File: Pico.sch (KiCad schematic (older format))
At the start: 5 parts, among them SW2801 SWITCH TACTILE SPST-NO 50MA 1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, U2801 Pico-JER

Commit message: Added PCA9745B16B. Updated schematic. ERC Passes.
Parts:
- U2801: symbol TMPCB_R2:Pico-JER -> Macro-Keyboard-rescue:Pico-JER-TMPCB_R2
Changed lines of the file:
@@
 L power:GND #PWR02809
 U 1 1 61A68B88
-P 6300 2850
-F 0 "#PWR02809" H 6300 2600 50  0001 C CNN
-F 1 "GND" V 6305 2722 50  0000 R CNN
-F 2 "" H 6300 2850 50  0001 C CNN
-F 3 "" H 6300 2850 50  0001 C CNN
-	1    6300 2850
+P 6650 2850
+F 0 "#PWR02809" H 6650 2600 50  0001 C CNN
+F 1 "GND" V 6655 2722 50  0000 R CNN
+F 2 "" H 6650 2850 50  0001 C CNN
+F 3 "" H 6650 2850 50  0001 C CNN
+	1    6650 2850
 	0    -1   -1   0
 $EndComp
@@
 	7500 3050 7500 2450
 Connection ~ 7500 3050
-Wire Wire Line
-	8200 2450 8200 2650
-Wire Wire Line
-	6300 2650 8200 2650
-Connection ~ 8200 2650
-Wire Wire Line
-	8200 2650 8200 3200
-$Comp
-L TMPCB_R2:Pico-JER U2801
+$Comp
+L Macro-Keyboard-rescue:Pico-JER-TMPCB_R2 U2801
 U 1 1 61A62316
 P 5600 3600
@@
 	0    -1   -1   0
 $EndComp
+Wire Wire Line
+	8200 2450 8200 2650
+Wire Wire Line
+	6300 2650 8200 2650
+Connection ~ 8200 2650
+Wire Wire Line
+	8200 2650 8200 3200
+Wire Wire Line
+	6300 2850 6550 2850
+$Comp
+L power:PWR_FLAG #FLG0101
+U 1 1 61A44DE2
+P 6550 2850
+F 0 "#FLG0101" H 6550 2925 50  0001 C CNN
+F 1 "PWR_FLAG" H 6550 3000 50  0000 C CNN
+F 2 "" H 6550 2850 50  0001 C CNN
+F 3 "~" H 6550 2850 50  0001 C CNN
+	1    6550 2850
+	1    0    0    -1
+$EndComp
+Connection ~ 6550 2850
+Wire Wire Line
+	6550 2850 6650 2850
 $EndSCHEMATC

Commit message: fixed broken schematics becuase of deleted rescue files. ECA passes.
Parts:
- U2801: symbol Macro-Keyboard-rescue:Pico-JER-TMPCB_R2 -> TMPCB_R2:Pico-JER
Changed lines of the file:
@@
 Connection ~ 7500 3050
 $Comp
-L Macro-Keyboard-rescue:Pico-JER-TMPCB_R2 U2801
+L TMPCB_R2:Pico-JER U2801
 U 1 1 61A62316
 P 5600 3600
+AR Path="/61A62316" Ref="U2801"  Part="1"
+AR Path="/61A0B536/61A62316" Ref="U2801"  Part="1"
 F 0 "U2801" H 6100 4750 50  0000 C CNN
 F 1 "Pico-JER" H 5050 4750 50  0000 C CNN
@@
 	8200 2650 8200 3200
 Wire Wire Line
-	6300 2850 6550 2850
+	6300 2850 6500 2850
 $Comp
-L power:PWR_FLAG #FLG0101
-U 1 1 61A44DE2
-P 6550 2850
-F 0 "#FLG0101" H 6550 2925 50  0001 C CNN
-F 1 "PWR_FLAG" H 6550 3000 50  0000 C CNN
-F 2 "" H 6550 2850 50  0001 C CNN
-F 3 "~" H 6550 2850 50  0001 C CNN
-	1    6550 2850
+L power:PWR_FLAG #FLG?
+U 1 1 61A20D92
+P 6500 2850
+F 0 "#FLG?" H 6500 2925 50  0001 C CNN
+F 1 "PWR_FLAG" H 6500 3023 50  0000 C CNN
+F 2 "" H 6500 2850 50  0001 C CNN
+F 3 "~" H 6500 2850 50  0001 C CNN
+	1    6500 2850
 	1    0    0    -1
 $EndComp
-Connection ~ 6550 2850
+Connection ~ 6500 2850
 Wire Wire Line
-	6550 2850 6650 2850
+	6500 2850 6650 2850
 $EndSCHEMATC

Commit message: initial layout
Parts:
- U2801: footprint RPi_Pico:RPi_Pico_SMD_TH -> TMPPCB_R2:RPi_Pico_SMD_TH-JER
- renumbered C2802 to C2801, C2803 to C2802
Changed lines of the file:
@@
 $EndDescr
 $Comp
-L power:GND #PWR02804
+L power:GND #PWR02801
 U 1 1 61A645F3
 P 4900 2850
-F 0 "#PWR02804" H 4900 2600 50  0001 C CNN
+F 0 "#PWR02801" H 4900 2600 50  0001 C CNN
 F 1 "GND" V 4905 2722 50  0000 R CNN
 F 2 "" H 4900 2850 50  0001 C CNN
@@
 $EndComp
 $Comp
-L power:GND #PWR02805
+L power:GND #PWR02802
 U 1 1 61A67A97
 P 4900 3350
-F 0 "#PWR02805" H 4900 3100 50  0001 C CNN
+F 0 "#PWR02802" H 4900 3100 50  0001 C CNN
 F 1 "GND" V 4905 3222 50  0000 R CNN
 F 2 "" H 4900 3350 50  0001 C CNN
@@
 $EndComp
 $Comp
-L power:GND #PWR02806
+L power:GND #PWR02803
 U 1 1 61A67DF9
 P 4900 3850
-F 0 "#PWR02806" H 4900 3600 50  0001 C CNN
+F 0 "#PWR02803" H 4900 3600 50  0001 C CNN
 F 1 "GND" V 4905 3722 50  0000 R CNN
 F 2 "" H 4900 3850 50  0001 C CNN
@@
 $EndComp
 $Comp
-L power:GND #PWR02807
+L power:GND #PWR02804
 U 1 1 61A681A5
 P 4900 4350
-F 0 "#PWR02807" H 4900 4100 50  0001 C CNN
+F 0 "#PWR02804" H 4900 4100 50  0001 C CNN
 F 1 "GND" V 4905 4222 50  0000 R CNN
 F 2 "" H 4900 4350 50  0001 C CNN
@@
 $EndComp
 $Comp
-L power:GND #PWR02808
+L power:GND #PWR02805
 U 1 1 61A6852A
 P 5600 4750
-F 0 "#PWR02808" H 5600 4500 50  0001 C CNN
+F 0 "#PWR02805" H 5600 4500 50  0001 C CNN
 F 1 "GND" H 5605 4577 50  0000 C CNN
 F 2 "" H 5600 4750 50  0001 C CNN
@@
 $EndComp
 $Comp
-L power:GND #PWR02811
+L power:GND #PWR02807
 U 1 1 61A69385
 P 6300 3850
-F 0 "#PWR02811" H 6300 3600 50  0001 C CNN
+F 0 "#PWR02807" H 6300 3600 50  0001 C CNN
 F 1 "GND" V 6305 3722 50  0000 R CNN
 F 2 "" H 6300 3850 50  0001 C CNN
@@
 $EndComp
 $Comp
-L power:GND #PWR02812
+L power:GND #PWR02808
 U 1 1 61A69B7B
 P 6300 4350
-F 0 "#PWR02812" H 6300 4100 50  0001 C CNN
+F 0 "#PWR02808" H 6300 4100 50  0001 C CNN
 F 1 "GND" V 6305 4222 50  0000 R CNN
 F 2 "" H 6300 4350 50  0001 C CNN
@@
 NoConn ~ 6300 2950
 $Comp
-L power:+3V3 #PWR02813
+L power:+3V3 #PWR02810
 U 1 1 61A6C23F
 P 7500 2450
-F 0 "#PWR02813" H 7500 2300 50  0001 C CNN
+F 0 "#PWR02810" H 7500 2300 50  0001 C CNN
 F 1 "+3V3" H 7515 2623 50  0000 C CNN
 F 2 "" H 7500 2450 50  0001 C CNN
@@
 $EndComp
 $Comp
-L power:GND #PWR02814
+L power:GND #PWR02811
 U 1 1 61A6EB26
 P 7500 3400
-F 0 "#PWR02814" H 7500 3150 50  0001 C CNN
+F 0 "#PWR02811" H 7500 3150 50  0001 C CNN
 F 1 "GND" H 7505 3227 50  0000 C CNN
 F 2 "" H 7500 3400 50  0001 C CNN
@@
 $EndComp
 $Comp
-L power:GND #PWR02817
+L power:GND #PWR02814
 U 1 1 61A6E775
 P 8200 3400
-F 0 "#PWR02817" H 8200 3150 50  0001 C CNN
+F 0 "#PWR02814" H 8200 3150 50  0001 C CNN
 F 1 "GND" H 8205 3227 50  0000 C CNN
 F 2 "" H 8200 3400 50  0001 C CNN
@@
 $EndComp
 $Comp
-L power:+5V #PWR02816
+L power:+5V #PWR02813
 U 1 1 61A6CFBC
 P 8200 2450
-F 0 "#PWR02816" H 8200 2300 50  0001 C CNN
+F 0 "#PWR02813" H 8200 2300 50  0001 C CNN
 F 1 "+5V" H 8215 2623 50  0000 C CNN
 F 2 "" H 8200 2450 50  0001 C CNN
@@
 Connection ~ 7500 3050
 $Comp
-L TMPCB_R2:Pico-JER U2801
+L TMPCB_R2:Pico-JER U?
 U 1 1 61A62316
 P 5600 3600
-AR Path="/61A62316" Ref="U2801"  Part="1"
+AR Path="/61A62316" Ref="U?"  Part="1"
 AR Path="/61A0B536/61A62316" Ref="U2801"  Part="1"
 F 0 "U2801" H 6100 4750 50  0000 C CNN
 F 1 "Pico-JER" H 5050 4750 50  0000 C CNN
-F 2 "RPi_Pico:RPi_Pico_SMD_TH" V 5600 3600 50  0001 C CNN
+F 2 "TMPPCB_R2:RPi_Pico_SMD_TH-JER" V 5600 3600 50  0001 C CNN
 F 3 "https://datasheets.raspberrypi.com/pico/pico-datasheet.pdf" H 5600 3600 50  0001 C CNN
 F 4 "2648-SC0915CT-ND" H 5600 3600 50  0001 C CNN "Digikey PN"
@@
 NoConn ~ 6300 2750
 $Comp
-L Device:C_Small C2802
+L Device:C_Small C2801
 U 1 1 61A6E1D1
 P 7500 3300
-F 0 "C2802" H 7592 3346 50  0000 L CNN
+F 0 "C2801" H 7592 3346 50  0000 L CNN
 F 1 "1 uF 10% 10V" H 7592 3255 50  0000 L CNN
 F 2 "Capacitor_SMD:C_0805_2012Metric_Pad1.18x1.45mm_HandSolder" H 7500 3300 50  0001 C CNN
@@
 $EndComp
 $Comp
-L Device:C_Small C2803
+L Device:C_Small C2802
 U 1 1 61A6D580
 P 8200 3300
-F 0 "C2803" H 8292 3346 50  0000 L CNN
+F 0 "C2802" H 8292 3346 50  0000 L CNN
 F 1 "1 uF 10% 10V" H 8292 3255 50  0000 L CNN
 F 2 "Capacitor_SMD:C_0805_2012Metric_Pad1.18x1.45mm_HandSolder" H 8200 3300 50  0001 C CNN
@@
 $EndComp
 $Comp
-L power:+3V3 #PWR02815
+L power:+3V3 #PWR02812
 U 1 1 61A78C6E
 P 7900 3900
-F 0 "#PWR02815" H 7900 3750 50  0001 C CNN
+F 0 "#PWR02812" H 7900 3750 50  0001 C CNN
 F 1 "+3V3" H 7915 4073 50  0000 C CNN
 F 2 "" H 7900 3900 50  0001 C CNN
@@
 Connection ~ 7900 4100
 $Comp
-L power:GND #PWR02818
+L power:GND #PWR02815
 U 1 1 61A79E42
 P 8950 4250
-F 0 "#PWR02818" H 8950 4000 50  0001 C CNN
+F 0 "#PWR02815" H 8950 4000 50  0001 C CNN
 F 1 "GND" H 8955 4077 50  0000 C CNN
 F 2 "" H 8950 4250 50  0001 C CNN
@@
 NoConn ~ 5700 4750
 $Comp
-L power:GND #PWR02810
+L power:GND #PWR02806
 U 1 1 61A7AE09
 P 6300 3350
-F 0 "#PWR02810" H 6300 3100 50  0001 C CNN
+F 0 "#PWR02806" H 6300 3100 50  0001 C CNN
 F 1 "GND" V 6305 3222 50  0000 R CNN
 F 2 "" H 6300 3350 50  0001 C CNN
@@
 	6300 2850 6500 2850
 $Comp
-L power:PWR_FLAG #FLG?
+L power:PWR_FLAG #FLG02801
 U 1 1 61A20D92
 P 6500 2850
-F 0 "#FLG?" H 6500 2925 50  0001 C CNN
+F 0 "#FLG02801" H 6500 2925 50  0001 C CNN
 F 1 "PWR_FLAG" H 6500 3023 50  0000 C CNN
 F 2 "" H 6500 2850 50  0001 C CNN

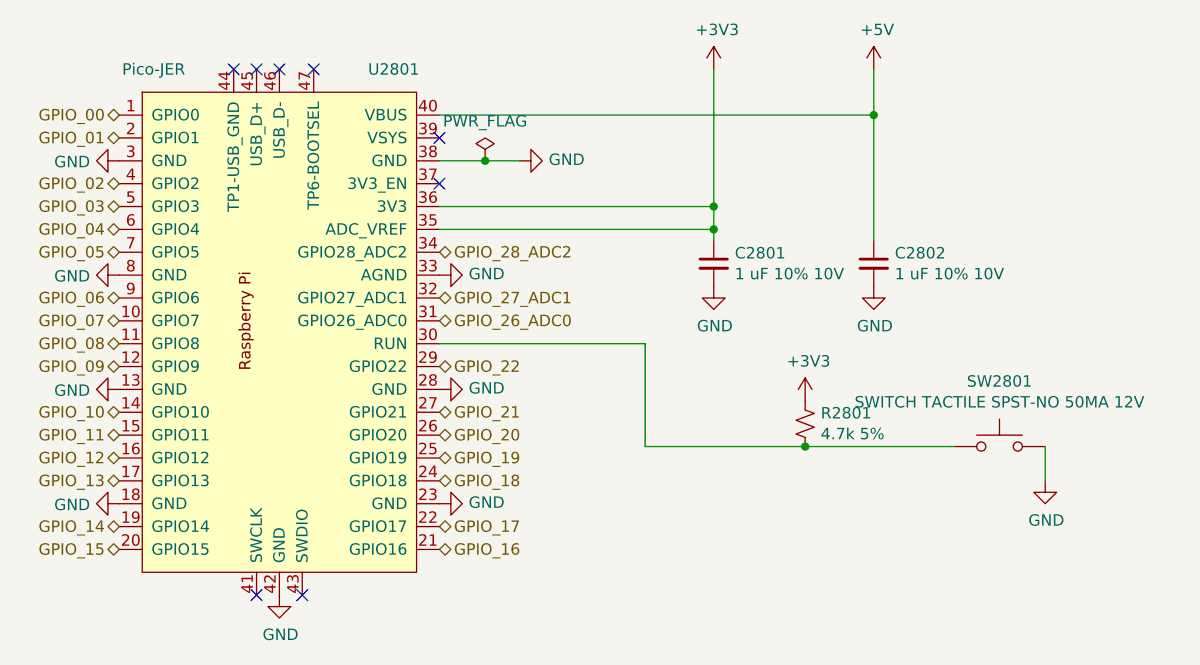
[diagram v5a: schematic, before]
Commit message: Add net labels and update PCB
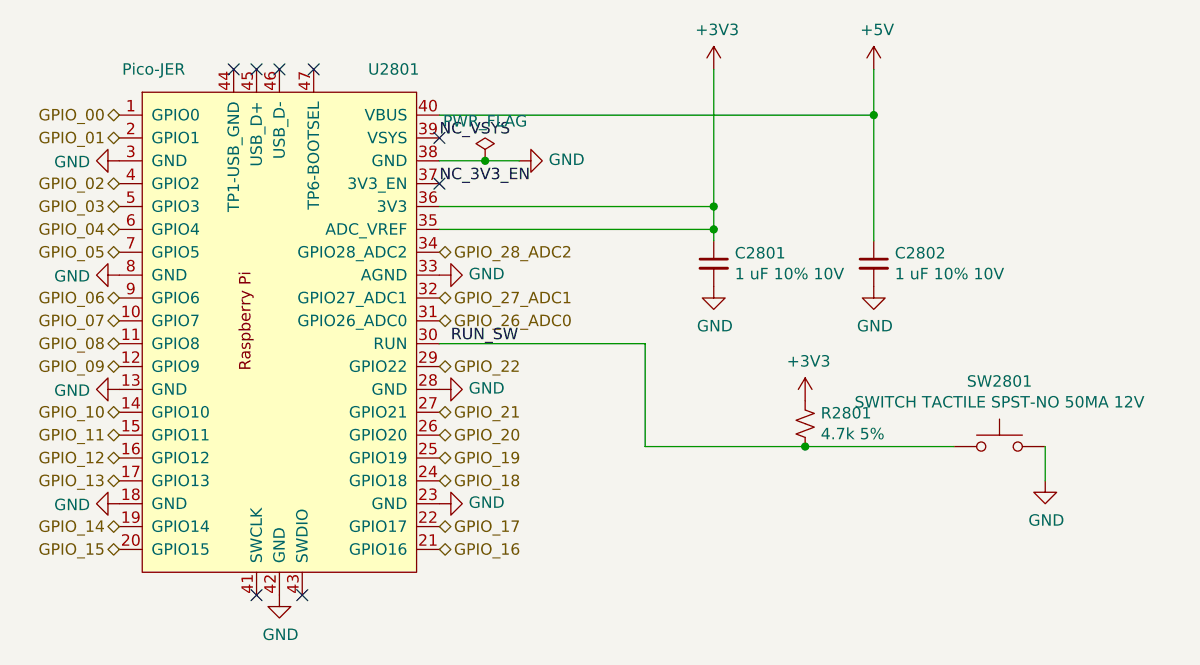
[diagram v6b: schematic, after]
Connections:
- net RUN_SW: now reaches R2801.2, SW2801.1, U2801.30 (RUN)
- net NC_3V3_EN: now reaches U2801.37 (3V3_EN)
- net NC_VSYS: now reaches U2801.39 (VSYS)
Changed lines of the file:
@@
 	1    0    0    -1
 $EndComp
+Text Label 6300 2750 0    50   ~ 0
+NC_VSYS
+Text Label 6300 2950 0    50   ~ 0
+NC_3V3_EN
+Text Label 6350 3650 0    50   ~ 0
+RUN_SW
 $EndSCHEMATC

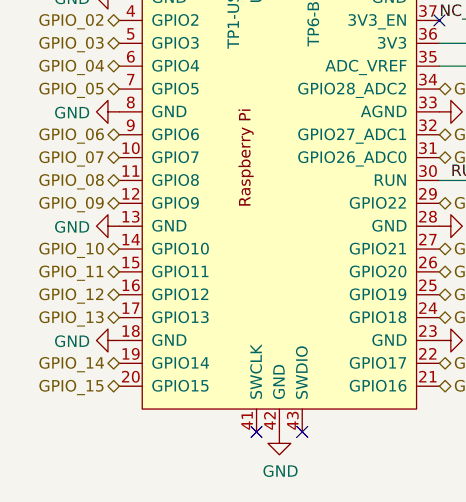
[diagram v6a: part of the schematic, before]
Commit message: Flipped pins on J2901 to be 24-1 instead of 1-24
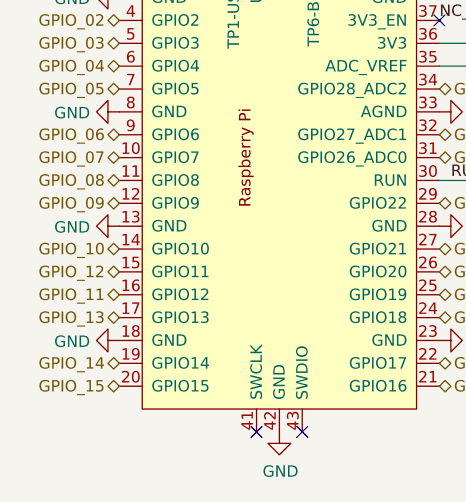
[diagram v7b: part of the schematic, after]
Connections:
- net GPIO_11: now also U2801.16 (GPIO12); no longer U2801.15 (GPIO11)
- net GPIO_12: now also U2801.15 (GPIO11); no longer U2801.16 (GPIO12)
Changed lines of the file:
@@
 GPIO_10
 Text HLabel 4900 4050 0    50   BiDi ~ 0
+GPIO_12
+Text HLabel 4900 4150 0    50   BiDi ~ 0
 GPIO_11
-Text HLabel 4900 4150 0    50   BiDi ~ 0
-GPIO_12
 Text HLabel 4900 4250 0    50   BiDi ~ 0
 GPIO_13

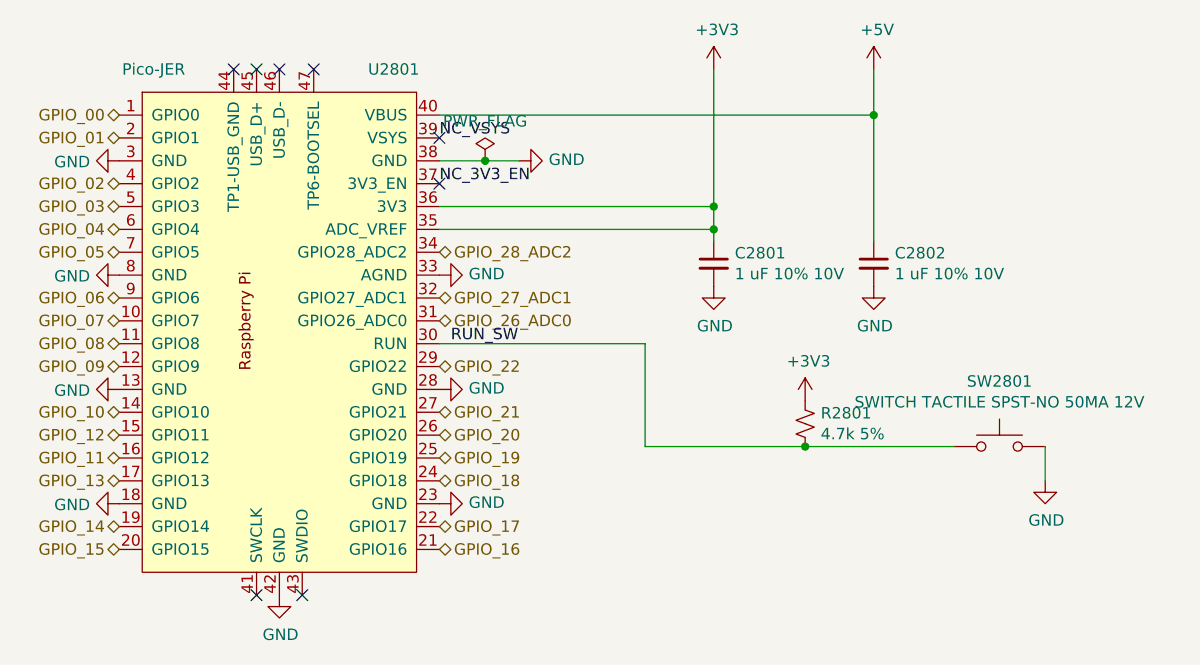
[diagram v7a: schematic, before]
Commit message: Fix design error in PI4ULS5V201TAEX. Reset and reassigned all annotations.
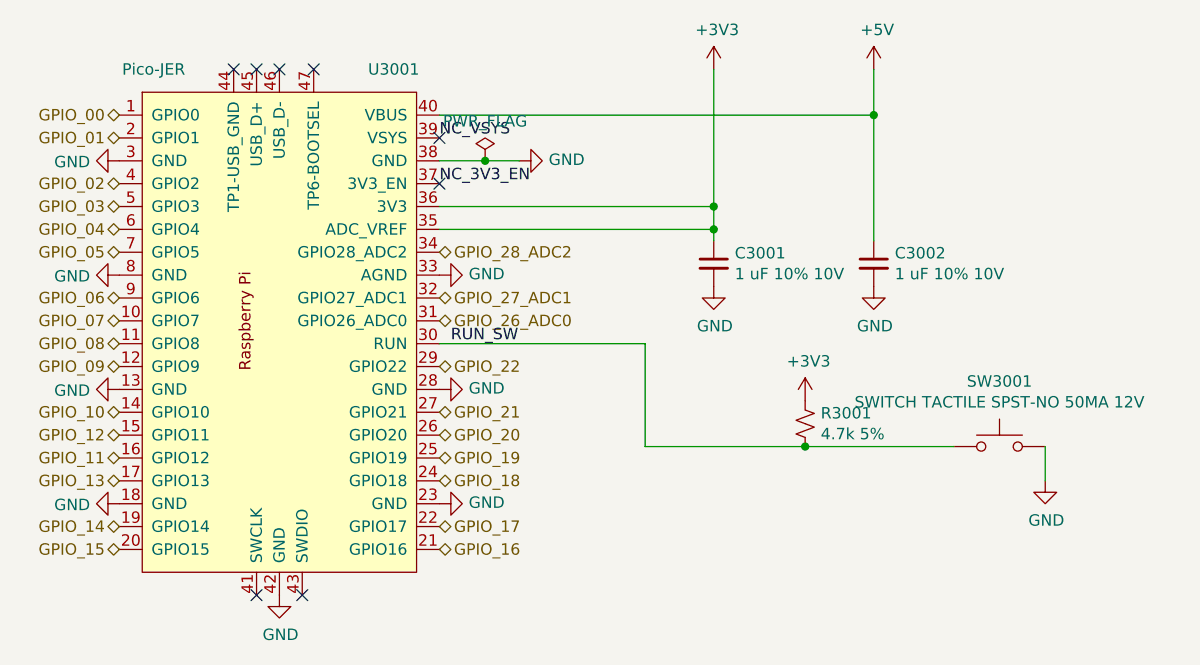
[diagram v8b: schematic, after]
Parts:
- renumbered C2801 to C3001, C2802 to C3002, R2801 to R3001, SW2801 to SW3001, U2801 to U3001
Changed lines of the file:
@@
 $EndDescr
 $Comp
-L power:GND #PWR02801
+L power:GND #PWR03001
 U 1 1 61A645F3
 P 4900 2850
-F 0 "#PWR02801" H 4900 2600 50  0001 C CNN
+F 0 "#PWR03001" H 4900 2600 50  0001 C CNN
 F 1 "GND" V 4905 2722 50  0000 R CNN
 F 2 "" H 4900 2850 50  0001 C CNN
@@
 $EndComp
 $Comp
-L power:GND #PWR02802
+L power:GND #PWR03002
 U 1 1 61A67A97
 P 4900 3350
-F 0 "#PWR02802" H 4900 3100 50  0001 C CNN
+F 0 "#PWR03002" H 4900 3100 50  0001 C CNN
 F 1 "GND" V 4905 3222 50  0000 R CNN
 F 2 "" H 4900 3350 50  0001 C CNN
@@
 $EndComp
 $Comp
-L power:GND #PWR02803
+L power:GND #PWR03003
 U 1 1 61A67DF9
 P 4900 3850
-F 0 "#PWR02803" H 4900 3600 50  0001 C CNN
+F 0 "#PWR03003" H 4900 3600 50  0001 C CNN
 F 1 "GND" V 4905 3722 50  0000 R CNN
 F 2 "" H 4900 3850 50  0001 C CNN
@@
 $EndComp
 $Comp
-L power:GND #PWR02804
+L power:GND #PWR03004
 U 1 1 61A681A5
 P 4900 4350
-F 0 "#PWR02804" H 4900 4100 50  0001 C CNN
+F 0 "#PWR03004" H 4900 4100 50  0001 C CNN
 F 1 "GND" V 4905 4222 50  0000 R CNN
 F 2 "" H 4900 4350 50  0001 C CNN
@@
 $EndComp
 $Comp
-L power:GND #PWR02805
+L power:GND #PWR03005
 U 1 1 61A6852A
 P 5600 4750
-F 0 "#PWR02805" H 5600 4500 50  0001 C CNN
+F 0 "#PWR03005" H 5600 4500 50  0001 C CNN
 F 1 "GND" H 5605 4577 50  0000 C CNN
 F 2 "" H 5600 4750 50  0001 C CNN
@@
 $EndComp
 $Comp
-L power:GND #PWR02809
+L power:GND #PWR03009
 U 1 1 61A68B88
 P 6650 2850
-F 0 "#PWR02809" H 6650 2600 50  0001 C CNN
+F 0 "#PWR03009" H 6650 2600 50  0001 C CNN
 F 1 "GND" V 6655 2722 50  0000 R CNN
 F 2 "" H 6650 2850 50  0001 C CNN
@@
 $EndComp
 $Comp
-L power:GND #PWR02807
+L power:GND #PWR03007
 U 1 1 61A69385
 P 6300 3850
-F 0 "#PWR02807" H 6300 3600 50  0001 C CNN
+F 0 "#PWR03007" H 6300 3600 50  0001 C CNN
 F 1 "GND" V 6305 3722 50  0000 R CNN
 F 2 "" H 6300 3850 50  0001 C CNN
@@
 $EndComp
 $Comp
-L power:GND #PWR02808
+L power:GND #PWR03008
 U 1 1 61A69B7B
 P 6300 4350
-F 0 "#PWR02808" H 6300 4100 50  0001 C CNN
+F 0 "#PWR03008" H 6300 4100 50  0001 C CNN
 F 1 "GND" V 6305 4222 50  0000 R CNN
 F 2 "" H 6300 4350 50  0001 C CNN
@@
 NoConn ~ 6300 2950
 $Comp
-L power:+3V3 #PWR02810
+L power:+3V3 #PWR03010
 U 1 1 61A6C23F
 P 7500 2450
-F 0 "#PWR02810" H 7500 2300 50  0001 C CNN
+F 0 "#PWR03010" H 7500 2300 50  0001 C CNN
 F 1 "+3V3" H 7515 2623 50  0000 C CNN
 F 2 "" H 7500 2450 50  0001 C CNN
@@
 $EndComp
 $Comp
-L power:GND #PWR02811
+L power:GND #PWR03011
 U 1 1 61A6EB26
 P 7500 3400
-F 0 "#PWR02811" H 7500 3150 50  0001 C CNN
+F 0 "#PWR03011" H 7500 3150 50  0001 C CNN
 F 1 "GND" H 7505 3227 50  0000 C CNN
 F 2 "" H 7500 3400 50  0001 C CNN
@@
 $EndComp
 $Comp
-L power:GND #PWR02814
+L power:GND #PWR03014
 U 1 1 61A6E775
 P 8200 3400
-F 0 "#PWR02814" H 8200 3150 50  0001 C CNN
+F 0 "#PWR03014" H 8200 3150 50  0001 C CNN
 F 1 "GND" H 8205 3227 50  0000 C CNN
 F 2 "" H 8200 3400 50  0001 C CNN
@@
 $EndComp
 $Comp
-L power:+5V #PWR02813
+L power:+5V #PWR03013
 U 1 1 61A6CFBC
 P 8200 2450
-F 0 "#PWR02813" H 8200 2300 50  0001 C CNN
+F 0 "#PWR03013" H 8200 2300 50  0001 C CNN
 F 1 "+5V" H 8215 2623 50  0000 C CNN
 F 2 "" H 8200 2450 50  0001 C CNN
@@
 P 5600 3600
 AR Path="/61A62316" Ref="U?"  Part="1"
-AR Path="/61A0B536/61A62316" Ref="U2801"  Part="1"
-F 0 "U2801" H 6100 4750 50  0000 C CNN
+AR Path="/61A0B536/61A62316" Ref="U3001"  Part="1"
+F 0 "U3001" H 6100 4750 50  0000 C CNN
 F 1 "Pico-JER" H 5050 4750 50  0000 C CNN
 F 2 "TMPPCB_R2:RPi_Pico_SMD_TH-JER" V 5600 3600 50  0001 C CNN
@@
 NoConn ~ 6300 2750
 $Comp
-L Device:C_Small C2801
+L Device:C_Small C3001
 U 1 1 61A6E1D1
 P 7500 3300
-F 0 "C2801" H 7592 3346 50  0000 L CNN
+F 0 "C3001" H 7592 3346 50  0000 L CNN
 F 1 "1 uF 10% 10V" H 7592 3255 50  0000 L CNN
 F 2 "Capacitor_SMD:C_0805_2012Metric_Pad1.18x1.45mm_HandSolder" H 7500 3300 50  0001 C CNN
@@
 $EndComp
 $Comp
-L Device:C_Small C2802
+L Device:C_Small C3002
 U 1 1 61A6D580
 P 8200 3300
-F 0 "C2802" H 8292 3346 50  0000 L CNN
+F 0 "C3002" H 8292 3346 50  0000 L CNN
 F 1 "1 uF 10% 10V" H 8292 3255 50  0000 L CNN
 F 2 "Capacitor_SMD:C_0805_2012Metric_Pad1.18x1.45mm_HandSolder" H 8200 3300 50  0001 C CNN
@@
 $EndComp
 $Comp
-L Device:R_Small_US R2801
+L Device:R_Small_US R3001
 U 1 1 61A781B3
 P 7900 4000
-F 0 "R2801" H 7968 4046 50  0000 L CNN
+F 0 "R3001" H 7968 4046 50  0000 L CNN
 F 1 "4.7k 5%" H 7968 3955 50  0000 L CNN
 F 2 "Resistor_SMD:R_0805_2012Metric_Pad1.20x1.40mm_HandSolder" H 7900 4000 50  0001 C CNN
@@
 $EndComp
 $Comp
-L power:+3V3 #PWR02812
+L power:+3V3 #PWR03012
 U 1 1 61A78C6E
 P 7900 3900
-F 0 "#PWR02812" H 7900 3750 50  0001 C CNN
+F 0 "#PWR03012" H 7900 3750 50  0001 C CNN
 F 1 "+3V3" H 7915 4073 50  0000 C CNN
 F 2 "" H 7900 3900 50  0001 C CNN
@@
 	7200 4100 7900 4100
 $Comp
-L Switch:SW_Push SW2801
+L Switch:SW_Push SW3001
 U 1 1 61A7983A
 P 8750 4100
-F 0 "SW2801" H 8750 4385 50  0000 C CNN
+F 0 "SW3001" H 8750 4385 50  0000 C CNN
 F 1 "SWITCH TACTILE SPST-NO 50MA 12V" H 8750 4294 50  0000 C CNN
 F 2 "Button_Switch_SMD:SW_SPST_TL3305A" H 8750 4300 50  0001 C CNN
@@
 Connection ~ 7900 4100
 $Comp
-L power:GND #PWR02815
+L power:GND #PWR03015
 U 1 1 61A79E42
 P 8950 4250
-F 0 "#PWR02815" H 8950 4000 50  0001 C CNN
+F 0 "#PWR03015" H 8950 4000 50  0001 C CNN
 F 1 "GND" H 8955 4077 50  0000 C CNN
 F 2 "" H 8950 4250 50  0001 C CNN
@@
 NoConn ~ 5700 4750
 $Comp
-L power:GND #PWR02806
+L power:GND #PWR03006
 U 1 1 61A7AE09
 P 6300 3350
-F 0 "#PWR02806" H 6300 3100 50  0001 C CNN
+F 0 "#PWR03006" H 6300 3100 50  0001 C CNN
 F 1 "GND" V 6305 3222 50  0000 R CNN
 F 2 "" H 6300 3350 50  0001 C CNN
@@
 Connection ~ 6500 2850
 $Comp
-L power:PWR_FLAG #FLG02801
+L power:PWR_FLAG #FLG03001
 U 1 1 61A20D92
 P 6500 2850
-F 0 "#FLG02801" H 6500 2925 50  0001 C CNN
+F 0 "#FLG03001" H 6500 2925 50  0001 C CNN
 F 1 "PWR_FLAG" H 6500 3023 50  0000 C CNN
 F 2 "" H 6500 2850 50  0001 C CNN
